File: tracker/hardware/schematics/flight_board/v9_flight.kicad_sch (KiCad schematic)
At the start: 46 parts, among them U1 ESP32-S3-WROOM-1U-N8R8, U2 LoRa2021F33-2G4, U3 LoRa2021_Castellated, U4 SX1280, U5 MAX-M10S, U6 MS5611-01BA, U7 TPS7A02

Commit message: docs(ssot): resolve the wing-orientation contradiction + register contested parameters
Part A — the live wing-orientation contradiction.
Governing record: docs/adr/049-wing-architecture.md §5 item 6 — the wing plane
is VERTICAL (a blade): long axis radial in the hub plane, 25 mm width vertical,
"resolved by arithmetic". Corroborated by ADR-046 §4.1 ("90 deg to the hub plane,
wing plane normal to the hub plane"), ADR-051 §1.4, ADR-055 §1 and
docs/analysis/wing-insolation-geometry.md §0.
Stale record: docs/WING-TO-HUB-SOCKET-SPEC.md §1 ("Wings 1–2 horizontal, 3–4
inclined ~30 deg below the hub plane", plus its self-contradicting "long axis is
perpendicular to the hub plane"), carried on by ADR-048 §5 item 6 / sheet
OPEN-23. §1's own declared authority is ADR-046, which says the opposite, so the
derivative prose is stale.
  - appended a CORRECTION to the socket spec §1 (body untouched) and a second one
    for its stale 22 x 22 hub figures;
  - appended a CORRECTION to ADR-048 (its datum and "footprint asserts no
    rotation" decision are explicitly UNCHANGED);
  - resolved sheet item OPEN-23 with the citation (keeps a TODO(unverified) for
    the wings 3-4 +/-30 deg droop, which stays open).
No engineering decision was re-made; precedence only.

Part B — the mechanism.
docs/ssot/parameters.json: a machine-readable single-source-of-truth registry of
the five contested parameters (8 MB flash; bare-LoRa2021 2.4 GHz RX; the ADR-049
wing orientation; the 103.0 x 103.0 mm hub outline; the 1.30 x 1.30 mm F33
castellation land). Each entry names ONE owning record, the canonical value,
anchors proving the owner still asserts it, a who-else-asserted note, a scan set,
reasoned exemptions and `forbid` regexes.
scripts/param_ssot_check.py: FAIL-CLOSED gate (0 PASS / 1 conflict / 2 cannot
determine; unreadable file, empty scan surface, un-reasoned exemption all fail).
Annotation-aware, so the repo's appended-correction convention passes.
tests/test_param_ssot.py: 14 tests incl. th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
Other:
- note added: "TODO(unverified) OPEN-23 WING ATTACH ORIENTATION — RESOLVED 2026-10-08 (ADR-049 s5 item 6) -- RESOLVED: the wing plane is VERTICAL (a blade) — long axis radial in the hub plane and pointing outward, 25 mm width vertical. Governing record: ADR-049 s5 item 6, resolved by the tab/slot arithmetic (ADR-046 s4.1: a 0.9 mm slot admits a 0.6 mm tab plus a 0.30 mm gap, and a 9.0 mm tab cannot fit a 6.0 mm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"
- note removed: "TODO(unverified) OPEN-23 ASSEMBLY ORIENTATION OF THE WING AT THE HUB (CONFLICTING RECORDS) -- Socket spec s1 says the wing's long axis is 'perpendicular to the hub plane' and then, in the next sentence, that wings 1-2 are 'horizontal' in the hub plane (and 3-4 inclined ~30 deg below it); ADR-046 s4.1 says '90 deg to the hub plane, wing plane normal to the hub plane'. The two readings cannot both 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"
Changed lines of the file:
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@@
 			(justify left bottom)
 		)
-	)	(text "TODO(unverified) OPEN-23 ASSEMBLY ORIENTATION OF THE WING AT THE HUB (CONFLICTING RECORDS) -- Socket spec s1 says the wing's long axis is 'perpendicular to the hub plane' and then, in the next sentence, that wings 1-2 are 'horizontal' in the hub plane (and 3-4 inclined ~30 deg below it); ADR-046 s4.1 says '90 deg to the hub plane, wing plane normal to the hub plane'. The two readings cannot both hold. TODO(unverified): the intended attach orientation, which the ADR-048 footprint deliberately does NOT assert - the land row, slot and keep-outs are laid out on a stated, newly decided datum (interface edge x slot centre line) and no rotation is fixed."
+	)	(text "TODO(unverified) OPEN-23 WING ATTACH ORIENTATION — RESOLVED 2026-10-08 (ADR-049 s5 item 6) -- RESOLVED: the wing plane is VERTICAL (a blade) — long axis radial in the hub plane and pointing outward, 25 mm width vertical. Governing record: ADR-049 s5 item 6, resolved by the tab/slot arithmetic (ADR-046 s4.1: a 0.9 mm slot admits a 0.6 mm tab plus a 0.30 mm gap, and a 9.0 mm tab cannot fit a 6.0 mm in-plane slot), corroborated by ADR-046 s4.1 ('90 deg to the hub plane, wing plane normal to the hub plane'), ADR-051 s1.4 and ADR-055 s1. The stale 'wings 1-2 horizontal' / 'long axis perpendicular to the hub plane' reading in WING-TO-HUB-SOCKET-SPEC s1 is v1-era prose (docs/hardware-design.md s3D-Assembly, an ANTENNA-coverage statement for a wing that carried a Yagi - V2-only and absent on v9, ADR-046 s2.4) and now carries an appended CORRECTION. The ADR-048 footprint's own decision is UNCHANGED: it asserts no rotation (datum = interface edge x slot centre line). Registered as 'wing_plane_orientation' in docs/ssot/parameters.json; gate scripts/param_ssot_check.py. STILL OPEN: TODO(unverified) whether the ~30 deg droop of wings 3-4 is retained on v9 - it had an antenna-coverage rationale only and no v9 record fixes it."
 		(exclude_from_sim no)
 		(at 30.48 434.34 0)

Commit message: feat(sch): SYMBOL SURGERY DONE -- 0 empty footprints (was 7), PVA off-board, U_CUT/HUB_CVT get real parts and pin counts
OPERATOR AUTHORISED THIS AND IT IS NOW APPLIED. The root cause of the 7 missing parts was measured
precisely: the schematic INSTANCES carried `(property "Footprint" "")` -- EMPTY -- while a working
instance (U2) carried `(property "Footprint" "balloon_flight_v9:LoRa2021F33_2G4")`. That empty
property is why the generator reported them "unplaceable" and they never reached the board.

RESULT, VERIFIED FROM THE REGENERATED NETLIST:
  empty footprints: 7 -> NONE
  total comps     : 46 -> 44 (PVA1/PVA2 correctly OFF the board)

=== 1. PVA1/PVA2 OFF-BOARD (operator: "keep them off board and rout them through the connector") ===
tracker/hardware/apply_pva_offboard.py sets `on_board no` + `in_bom no` on both cells. NOT a footprint
invention -- the faithful reading of the ruling: the part stops being a PCBA placement (so it is no
longer "unplaceable") and leaves the ORDER BOM, becoming a MECHANICAL DRAWING, the operator's own
words. `dnp` is left alone because "do not populate" is a different statement from "not on this board
at all", and the Value stays SolarCell_78x39mm so the drawing identity is preserved. The string
topology is UNTOUCHED: D_HUB1/D_HUB2 stay on the PCBA and the netlist's
HUB_PV_P -> D_HUB1 -> HUB_PV_MID1 -> D_HUB2 -> HUB_PV_N chain is unchanged, with the cells terminating
at the connector exactly as the wing solar already does at J_W1..J_W4.

=== 2. CUT_CHANNEL 3 -> 6 pins, and a REAL PART ===
Picked on price and fit, evidence in docs/fab/CUT-DRIVER-SELECTION.md:
    CUT_CHANNEL -> SN74LVC1G373DBVR  LCSC C128413  stock 34892  $0.2779  SOT-23-6
Pin contract: 1 VSCAP, 2 GND, 3 CUT_W (ALL THREE UNCHANGED) + 4 ARM, 5 CTRL, 6 SENSE.
THE CHANGE IS ADDITIVE ON PURPOSE: KiCad connects by COORDINATE, so moving or renumbering an existing
pin would silently detach wires already drawn to it. Pins 1-3 keep their exact coordinates and names;
the new 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
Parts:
- PVA1, PVA2: now left out of the parts list
- U_CUT1, U_CUT2, U_CUT3, U_CUT4: value latched cut driver + cut-sense (part TODO(unverified)) -> SN74LVC1G373DBVR; footprint (none) -> Package_TO_SOT_SMD:SOT-23-6; LCSC (none) -> C128413
- U_HUB_CVT: value HUB_PV input (part TODO(unverified)) -> BQ25504RGTR; footprint (none) -> Package_DFN_QFN:VQFN-16-1EP_3x3mm_P0.5mm_EP1.1x1.1mm; LCSC (none) -> C2876746
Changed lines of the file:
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@@
 		(unit 1)
 		(exclude_from_sim no)
-		(in_bom yes)
-		(on_board yes)
+		(in_bom no)
+		(on_board no)
 		(dnp no)
 		(property "Reference" "PVA1"
@@
 		(unit 1)
 		(exclude_from_sim no)
-		(in_bom yes)
-		(on_board yes)
+		(in_bom no)
+		(on_board no)
 		(dnp no)
 		(property "Reference" "PVA2"
@@
 			)
 		)
-		(property "Value" "HUB_PV input (part TODO(unverified))"
+		(property "Value" "BQ25504RGTR"
 			(at 670.56 165.1 0)
 			(effects
@@
 			)
 		)
-		(property "Footprint" ""
+		(property "Footprint" "Package_DFN_QFN:VQFN-16-1EP_3x3mm_P0.5mm_EP1.1x1.1mm"
 			(at 668.02 162.56 0)
 			(effects
@@
 			)
 		)
+		(property "LCSC" "C2876746"
+			(at 0 0 0)
+			(effects
+				(font
+					(size 1.27 1.27)
+				)
+				(hide yes)
+			)
+		)
 		(pin "1"
 		)
@@
 		)
 		(pin "3"
+		)
+		(pin "4"
 		)
 		(instances
@@
 			)
 		)
-		(property "Value" "latched cut driver + cut-sense (part TODO(unverified))"
+		(property "Value" "SN74LVC1G373DBVR"
 			(at 670.56 198.12 0)
 			(effects
@@
 			)
 		)
-		(property "Footprint" ""
+		(property "Footprint" "Package_TO_SOT_SMD:SOT-23-6"
 			(at 668.02 195.58 0)
 			(effects
@@
 			)
 		)
+		(property "LCSC" "C128413"
+			(at 0 0 0)
+			(effects
+				(font
+					(size 1.27 1.27)
+				)
+				(hide yes)
+			)
+		)
 		(pin "1"
 		)
@@
 		)
 		(pin "3"
+		)
+		(pin "4"
+		)
+		(pin "5"
+		)
+		(pin "6"
 		)
 		(instances
@@
 			)
 		)
-		(property "Value" "latched cut driver + cut-sense (part TODO(unverified))"
+		(property "Value" "SN74LVC1G373DBVR"
 			(at 670.56 231.14 0)
 			(effects
@@
 			)
 		)
-		(property "Footprint" ""
+		(property "Footprint" "Package_TO_SOT_SMD:SOT-23-6"
 			(at 668.02 228.6 0)
 			(effects
@@
 			)
 		)
+		(property "LCSC" "C128413"
+			(at 0 0 0)
+			(effects
+				(font
+					(size 1.27 1.27)
+				)
+				(hide yes)
+			)
+		)
 		(pin "1"
 		)
@@
 		)
 		(pin "3"
+		)
+		(pin "4"
+		)
+		(pin "5"
+		)
+		(pin "6"
 		)
 		(instances
@@
 			)
 		)
-		(property "Value" "latched cut driver + cut-sense (part TODO(unverified))"
+		(property "Value" "SN74LVC1G373DBVR"
 			(at 670.56 264.16 0)
 			(effects
@@
 			)
 		)
-		(property "Footprint" ""
+		(property "Footprint" "Package_TO_SOT_SMD:SOT-23-6"
 			(at 668.02 261.62 0)
 			(effects
@@
 			)
 		)
+		(property "LCSC" "C128413"
+			(at 0 0 0)
+			(effects
+				(font
+					(size 1.27 1.27)
+				)
+				(hide yes)
+			)
+		)
 		(pin "1"
 		)
@@
 		)
 		(pin "3"
+		)
+		(pin "4"
+		)
+		(pin "5"
+		)
+		(pin "6"
 		)
 		(instances
@@
 			)
 		)
-		(property "Value" "latched cut driver + cut-sense (part TODO(unverified))"
+		(property "Value" "SN74LVC1G373DBVR"
 			(at 670.56 297.18 0)
 			(effects
@@
 			)
 		)
-		(property "Footprint" ""
+		(property "Footprint" "Package_TO_SOT_SMD:SOT-23-6"
 			(at 668.02 294.64 0)
 			(effects
@@
 			)
 		)
+		(property "LCSC" "C128413"
+			(at 0 0 0)
+			(effects
+				(font
+					(size 1.27 1.27)
+				)
+				(hide yes)
+			)
+		)
 		(pin "1"
 		)
@@
 		(pin "3"
 		)
-		(instances
+		(pin "4"
+		)
+		(pin "5"
+		)
+		(pin "6"
+		)
+		(instances

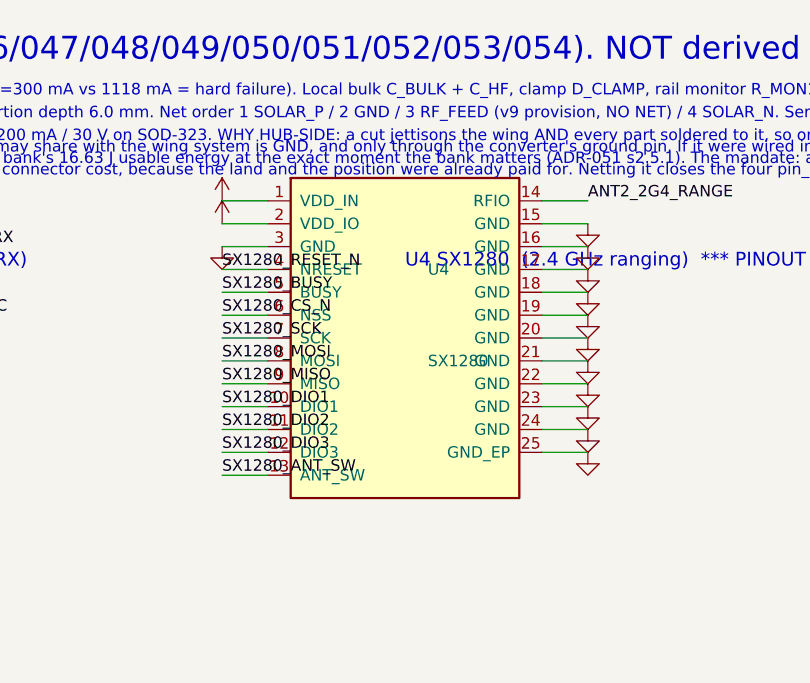
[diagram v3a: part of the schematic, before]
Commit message: fix(sch): STEP 1 -- SX1280 symbol rewritten to the REAL pinout; the block would not parse because `bidi` is not a KiCad pin type
THE SYMBOL NOW MATCHES THE PART
Real names, numbers and sides, from Semtech SX1280/SX1281 Data Sheet Rev 3.2 (March 2020) Table 2-1
and Figure 2-1, vendored at docs/sx1280/. Sides 6/3/9/6 = LEFT 1-6, BOTTOM 7-9, RIGHT 10-18,
TOP 19-24, exposed pad 0 centre.

WHY EVERY EARLIER ATTEMPT FAILED TO LOAD
`bidi` IS NOT A VALID KICAD PIN ELECTRICAL TYPE. The correct token is `bidirectional`. KiCad reports
only "Failed to load schematic" with no line number, so this was found by PROBING each candidate type
against a known-good file:
    bidi -> FAILS
    bidirectional, passive, input, output, power_in, power_out, tri_state, free, unspecified,
    no_connect, open_collector, open_emitter -> PARSE
A single invalid enum value was the whole cause. Recorded because it costs no tokens to re-check and
infinite tokens to re-derive.

THE OUTPUT IS NOW VALIDATED BEFORE IT IS WRITTEN
Six earlier attempts each wrote a broken file and reported success. The generator now ASSERTS:
  * paren balance == 0 for the whole document and for the new block (the worst attempt was 97
    missing ")" -- CLOSES had been scraped from the pin template, so it ended at the PIN's close and
    never closed the unit or the symbol)
  * non-negative depth throughout
  * the per-line TAB PROFILE of every generated pin equals the source template's
Refuses to write on any failure.

WHAT THE CORRECTION ACTUALLY DID TO U4 (netlist evidence)
KiCad connects by PIN NUMBER, so installing the real table re-lands the existing wires on the real
pins -- and 13 nets collapse to 7:
    +3V3            pins 1,2  -> pin 1  = VR_PA
    /SX1280_RESET_N pin 4     -> pin 2  = VDD_IN
    /SX1280_CS_N    pin 6     -> pin 3  = NRESET
    /SX1280_MOSI    pin 8     -> pin 4  = XTA
    /SX1280_DIO1    pin 10    -> pin 5  = GND
    /SX1280_DIO3    pin 12    -> pin 6  = XTB
    GND             12 pins   -> pin 1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
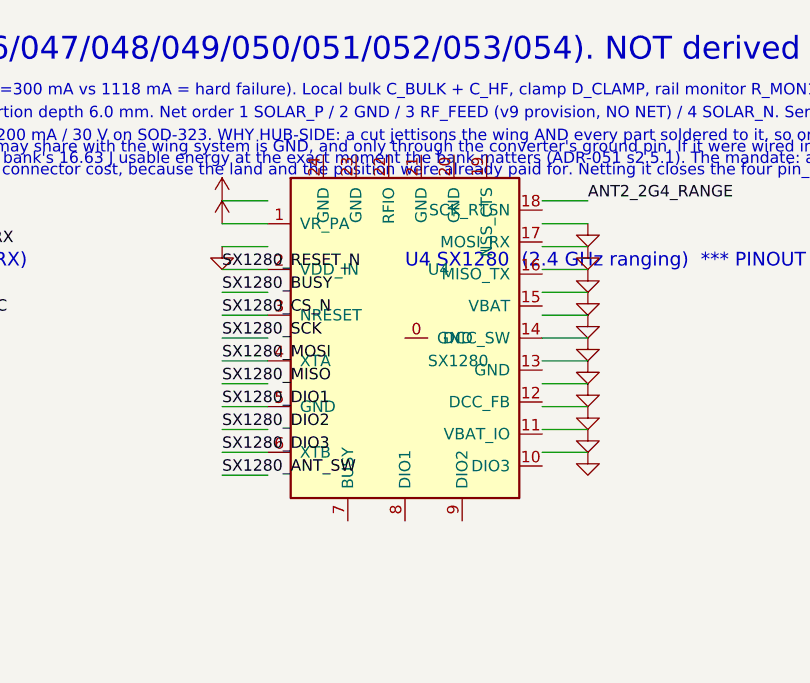
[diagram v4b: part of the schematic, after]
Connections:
- net +3V3: no longer U4.2 (VDD_IO)
- net ANT2_2G4_RANGE: no longer U4.14 (RFIO)
- net GND: now also U4.14 (DCC_SW); no longer U4.15 (GND), U4.16 (GND), U4.17 (GND), U4.18 (GND), U4.19 (GND), U4.20 (GND), U4.21 (GND), U4.22 (GND), U4.23 (GND), U4.24 (GND), U4.25 (GND_EP), U4.3 (GND)
- net SX1280_ANT_SW: no longer U4.13 (ANT_SW)
- net SX1280_BUSY: no longer U4.5 (BUSY)
- net SX1280_CS_N: now also U4.3 (NRESET); no longer U4.6 (NSS)
- net SX1280_DIO1: now also U4.5 (GND); no longer U4.10 (DIO1)
- net SX1280_DIO2: no longer U4.11 (DIO2)
- net SX1280_DIO3: now also U4.6 (XTB); no longer U4.12 (DIO3)
- net SX1280_MISO: no longer U4.9 (MISO)
- net SX1280_MOSI: now also U4.4 (XTA); no longer U4.8 (MOSI)
- net SX1280_RESET_N: now also U4.2 (VDD_IN); no longer U4.4 (NRESET)
- net SX1280_SCK: no longer U4.7 (SCK)
